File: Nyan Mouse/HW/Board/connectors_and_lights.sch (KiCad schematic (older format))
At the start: 49 parts

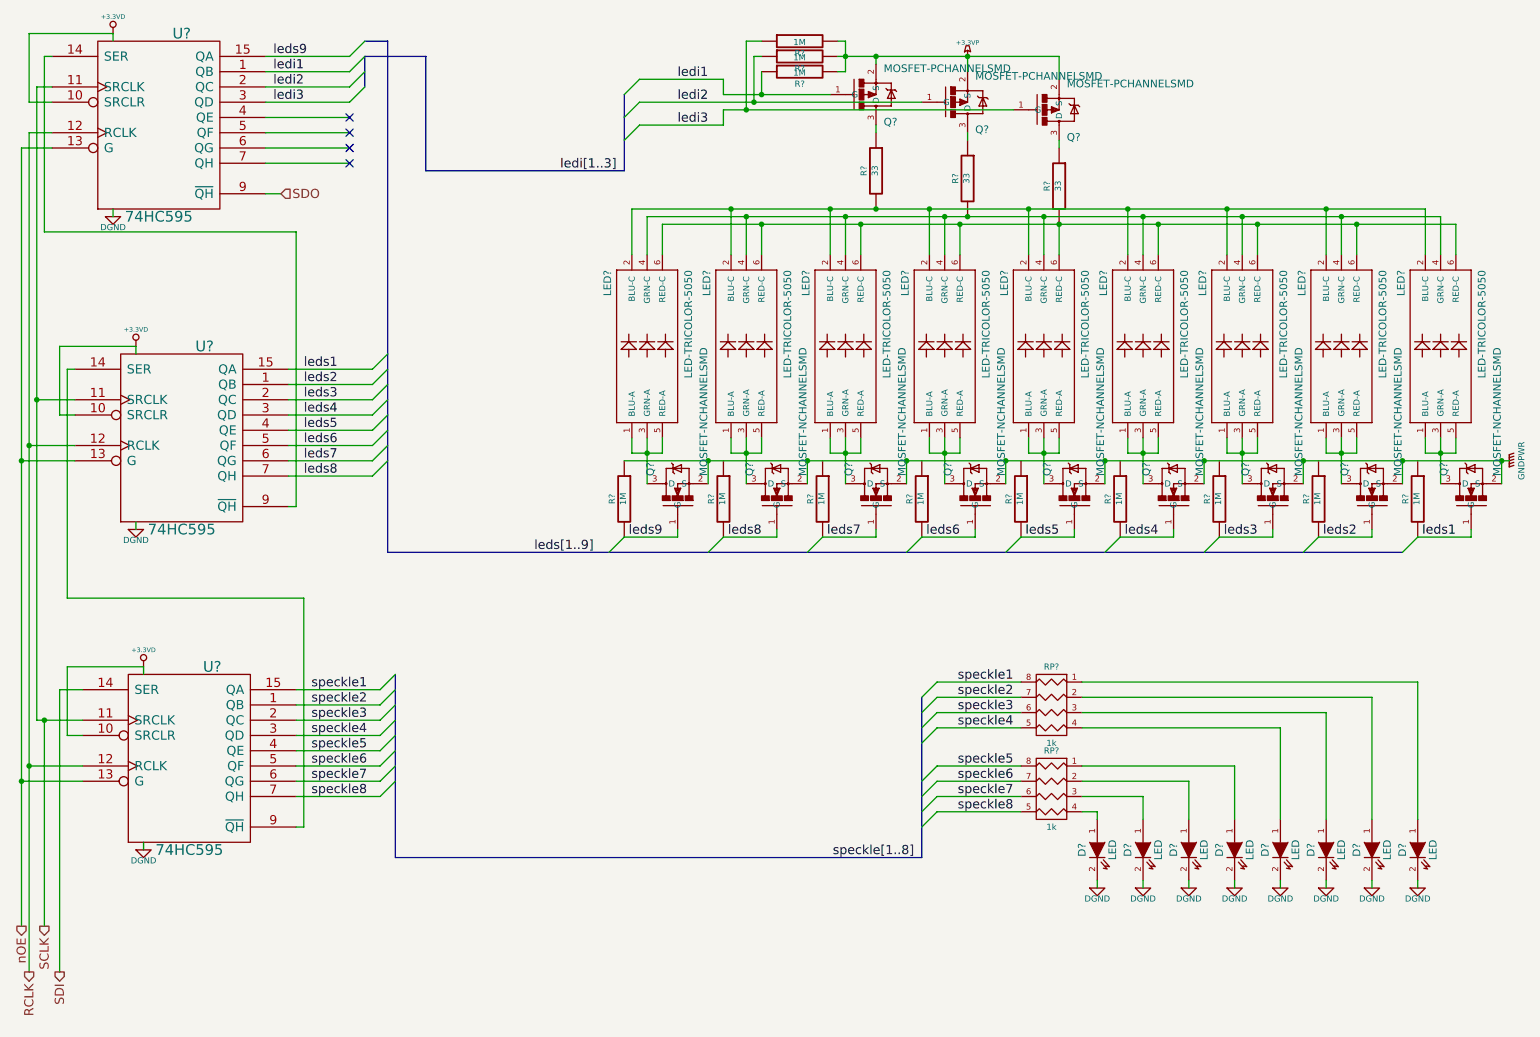
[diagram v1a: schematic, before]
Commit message: Changed DRV8837, Almost completed main board. ERC almost successful.
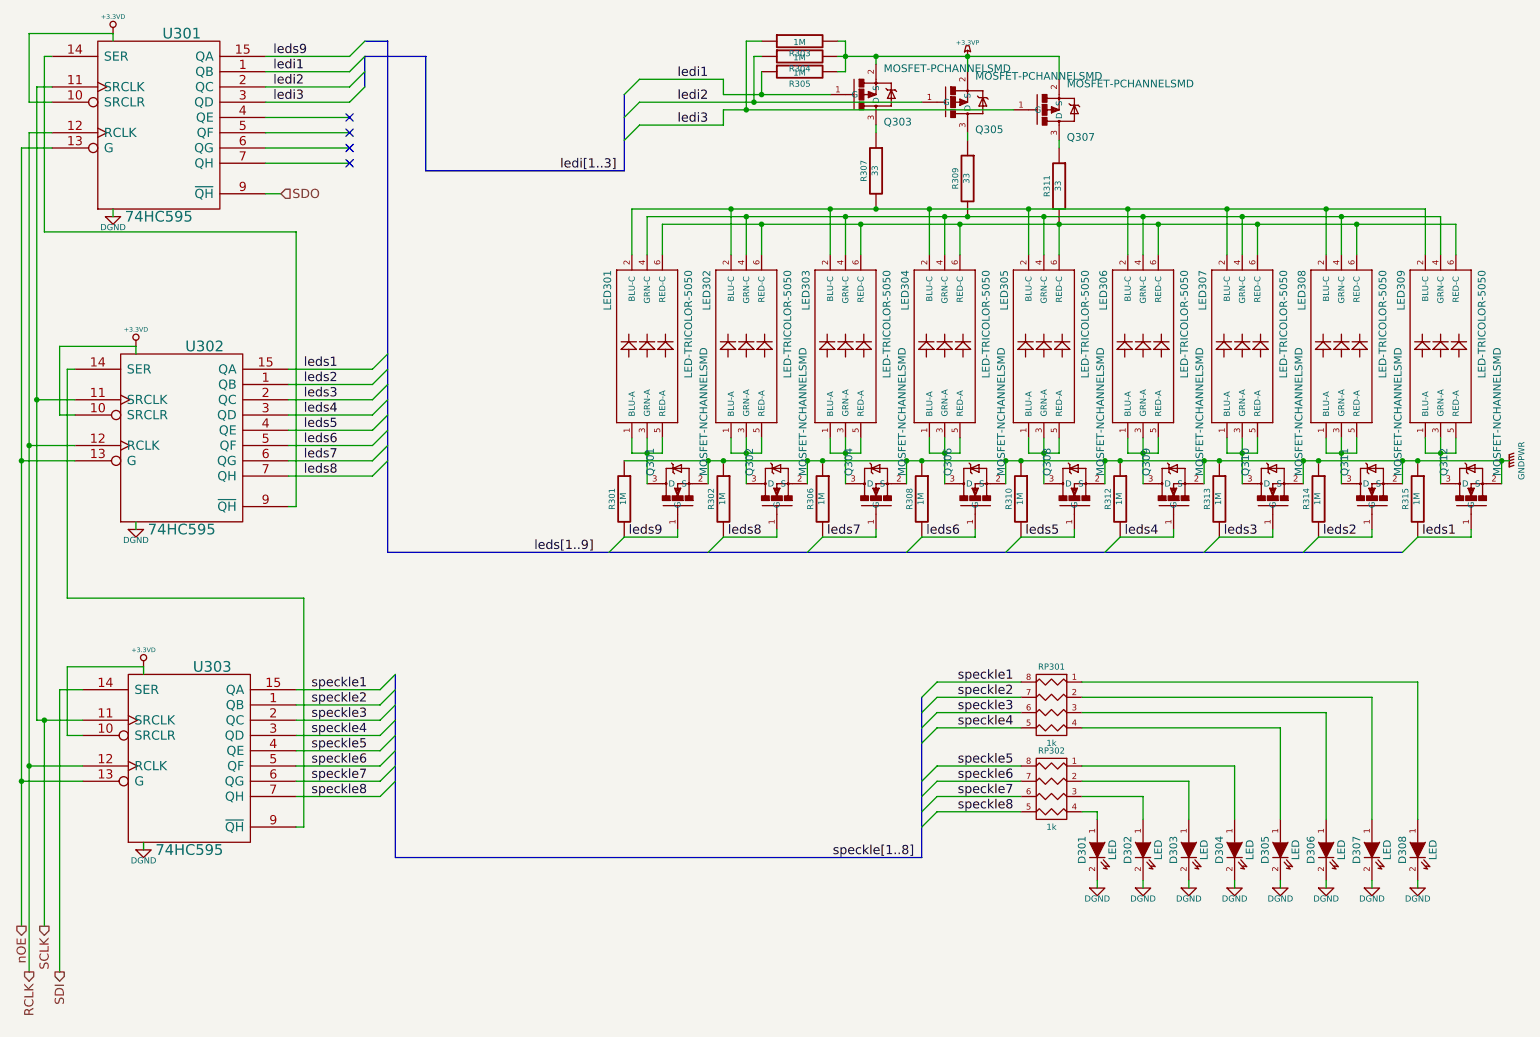
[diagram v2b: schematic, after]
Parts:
- gave numbers to parts that had none: 49
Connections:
- net GNDPWR: now also R302.1, R306.1, R308.1, R310.1, R312.1, R313.1, R314.1, R315.1
